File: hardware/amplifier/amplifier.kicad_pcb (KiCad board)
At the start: 2 copper layers, 52.4 x 41.4 mm, 13 parts, among them K1 Out, P1 Sensor, P2 Pwr, U1 AD8223, U2 LT1010

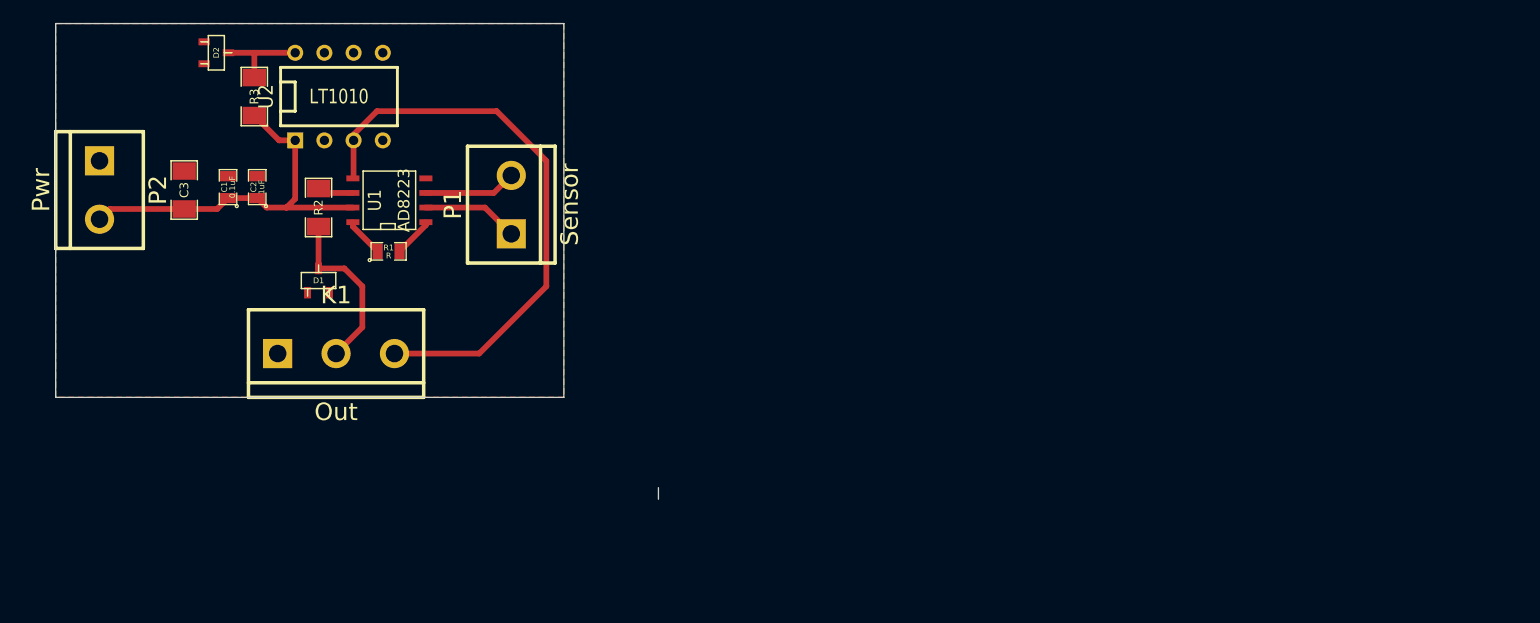
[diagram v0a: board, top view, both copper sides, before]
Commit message: Amplifier board: change instrumentation amplifier for INA2128.
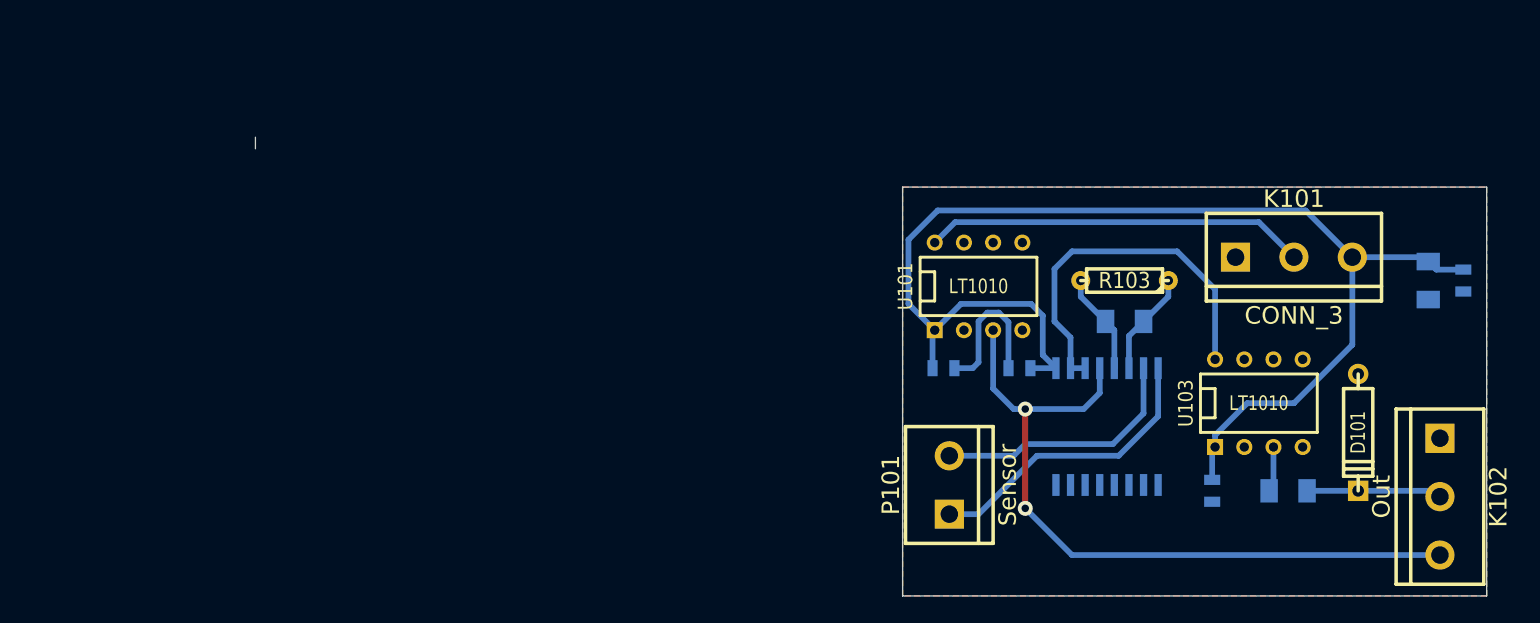
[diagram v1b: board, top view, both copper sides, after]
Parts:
- removed C1: 0.1uF, SM0805
- removed C2: 1uF, SM0805
- removed C3: 10uF, SM1206
- removed D1, D2: ZENER, sot23
- removed K1: Out, bornier3
- removed P1: Sensor, bornier2
- removed P2: Pwr, bornier2
- removed R1: R, SM0805
- removed R2, R3: 10K, SM1206
- removed U1: AD8223, SO8N
- removed U2: LT1010, DIP-8__300
- added C101: 0.1uF, SM0805, B.Cu at (296.2, 144.3)
- added C102: 1uF, SM0805, B.Cu at (318.0, 126.0)
- added C103: 10uF, SM1206, B.Cu at (315.0, 126.0)
- added C104: 0.1uF, SM0805, B.Cu at (279.4, 133.6)
- added C105: 0.1uF, SM0805, B.Cu at (272.8, 133.6)
- added D101: 1N4732, D4, F.Cu at (308.9, 139.2)
- added K101: CONN_3, bornier3, F.Cu at (303.3, 124.0)
- added K102: Out, bornier3, F.Cu at (316.0, 144.8)
- added P101: Sensor, bornier2, F.Cu at (273.3, 143.8)
- added R101: 1K, SM1206, B.Cu at (302.8, 144.3)
- added R102: R, SM1206, B.Cu at (288.5, 129.5)
- added R103: R, R3-LARGE_PADS, F.Cu at (288.5, 126.0)
- added U101: LT1010, DIP-8__300, F.Cu at (275.8, 126.5)
- added U102: INA2128, SO16L, B.Cu at (287.0, 138.7)
- added U103: LT1010, DIP-8__300, F.Cu at (300.2, 136.7)
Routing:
- net VDD: track 33.7 -> 108.5 mm
- net /VrefIN: track 0.00 -> 33.2 mm
- net N-000006: track 0.00 -> 32.5 mm
- net /Se2: track 8.38 -> 25.9 mm
- net /Vref: track 49.8 -> 64.2 mm, vias 0 -> 2
- net /Se1: track 8.06 -> 22.4 mm
- net GND: track 0.00 -> 13.1 mm
- net N-0000027: track 0.00 -> 9.04 mm
- net N-0000024: track 0.00 -> 8.83 mm
- net N-0000010: track 7.96 -> 0.00 mm
- net N-0000015: track 0.00 -> 3.97 mm
- net N-000002: track 3.49 -> 0.00 mm
- net N-000004: track 3.43 -> 0.00 mm
- net N-000001: track 3.14 -> 0.00 mm
- net /Vout: track 14.9 -> 11.8 mm
- added copper zone on B.Cu, net GND
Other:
- board size 52.4 x 41.4 mm -> 107.1 x 39.9 mm
- net class Default: via_dia 0.889 -> 1.3005; via_drill 0.635 -> 0.8992

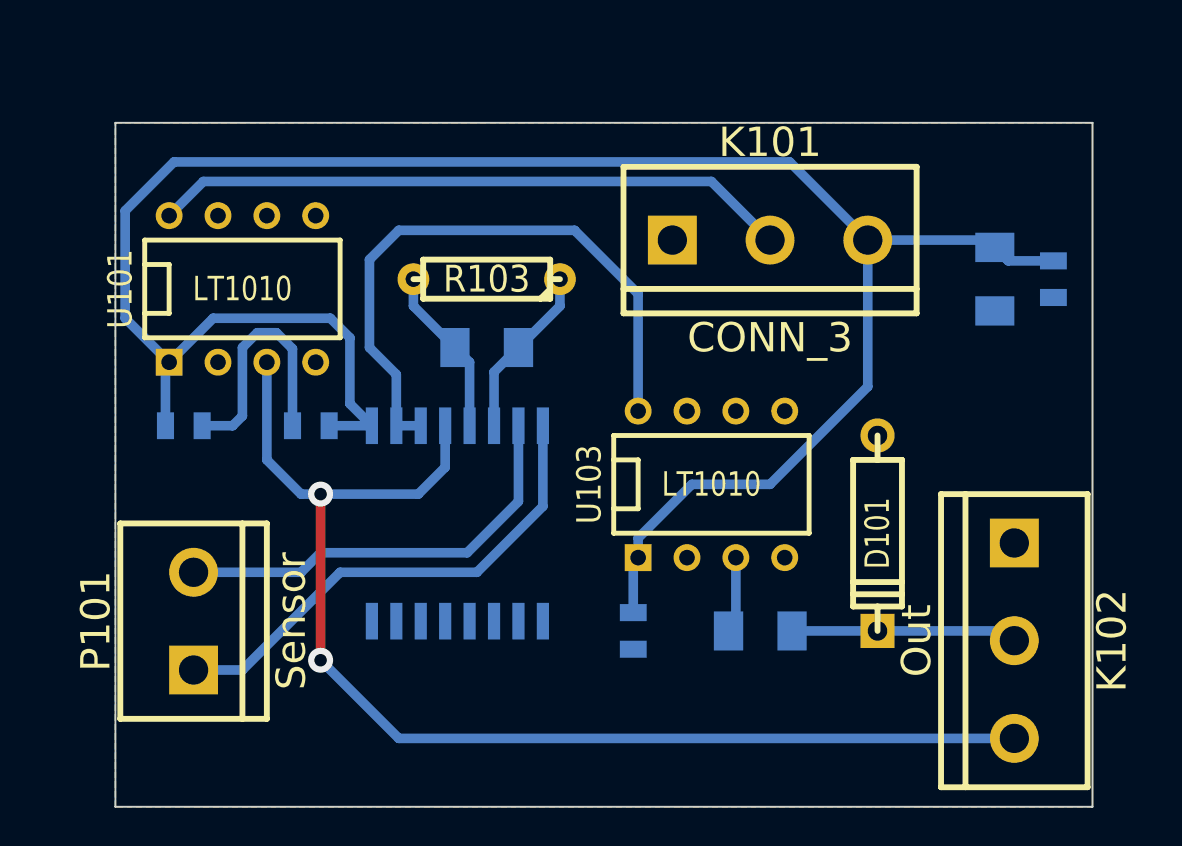
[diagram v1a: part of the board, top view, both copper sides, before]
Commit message: Moved power connector.
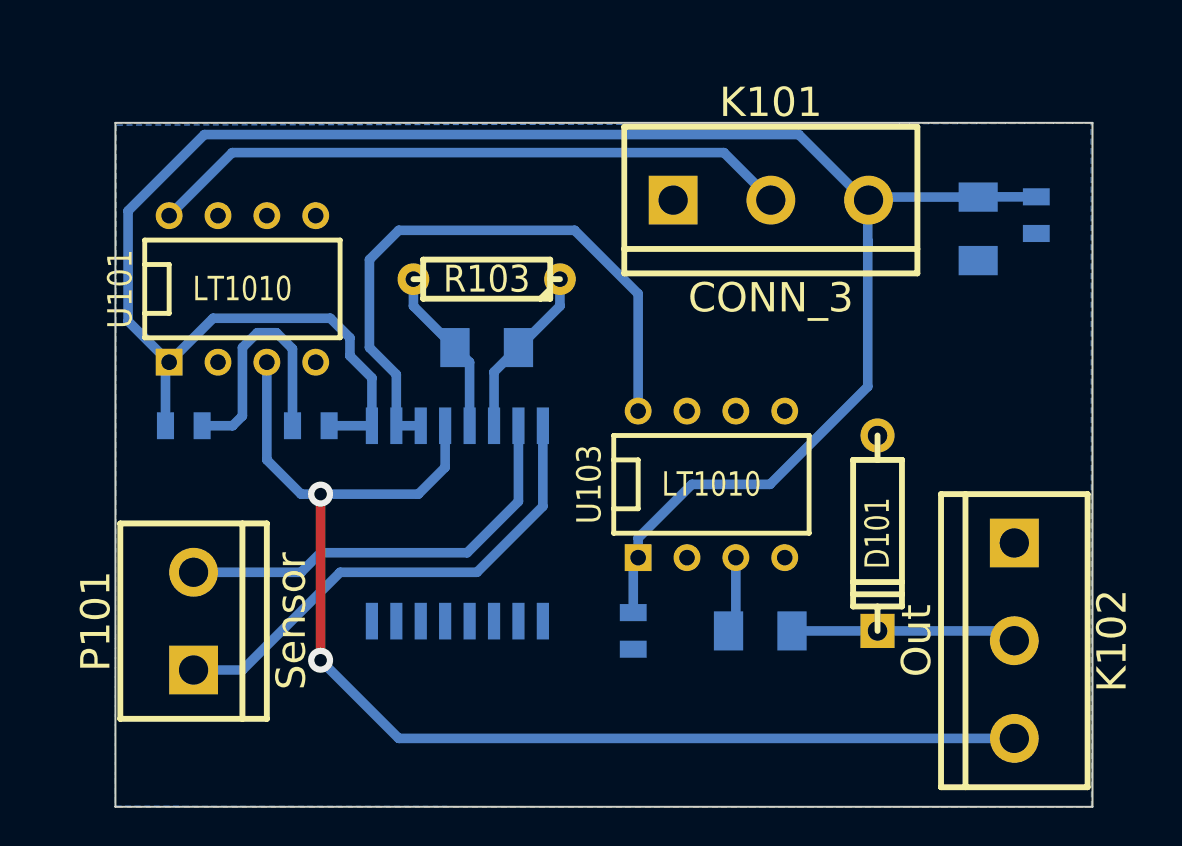
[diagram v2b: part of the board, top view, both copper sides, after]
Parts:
- moved C102 3.44 mm to (317.1, 122.7)
- moved C103 2.76 mm to (314.1, 123.4)
- moved K101 2.08 mm to (303.3, 121.9)
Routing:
- net VDD: track 108.5 -> 109.8 mm
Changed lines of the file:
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@@
-(kicad_pcb (version 3) (host pcbnew "(2013-jul-07)-stable")
+(kicad_pcb (version 3) (host pcbnew "(2013-07-07 BZR 4022)-stable")
   (general
     (links 32)
     (no_connects 0)
-    (area 212.897999 113.469999 212.998001 114.570001)
+    (area 212.897999 110.942001 335.66 153.466001)
     (thickness 1.6)
     (drawings 7)
-    (tracks 76)
+    (tracks 82)
     (zones 0)
     (modules 15)
@@
   (page A3)
   (layers
-    (15 F.Cu signal)
+    (15 F.Cu signal hide)
     (0 B.Cu signal)
     (16 B.Adhes user)
@@
   )
   (module SM1206 (layer B.Cu)
-    (at 314.96 125.984 270)
+    (at 314.0964 123.3678 270)
     (attr smd)
     (fp_text reference C103 (at 0 0 270) (layer B.SilkS)
@@
   )
   (module SM0805 (layer B.Cu)
-    (at 318.008 125.984 270)
+    (at 317.119 122.6566 270)
     (attr smd)
     (fp_text reference C102 (at 0 0.3175 270) (layer B.SilkS)
@@
   )
   (module bornier3 (layer F.Cu)
-    (at 303.276 123.952)
+    (at 303.31664 121.87428)
     (descr "Bornier d'alimentation 3 pins")
     (tags DEV)
@@
   (segment (start 279.908 137.16) (end 284.988 137.16) (width 0.5) (layer B.Cu) (net 4))
   (segment (start 277.114 135.382) (end 278.892 137.16) (width 0.5) (layer B.Cu) (net 4))
-  (segment (start 272.034 122.682) (end 273.812 120.904) (width 0.5) (layer B.Cu) (net 5))
-  (segment (start 300.228 120.904) (end 303.276 123.952) (width 0.5) (layer B.Cu) (net 5))
-  (segment (start 273.812 120.904) (end 300.228 120.904) (width 0.5) (layer B.Cu) (net 5))
+  (segment (start 303.31664 121.87428) (end 303.31664 121.8438) (width 0.5) (layer B.Cu) (net 5))
+  (segment (start 275.3106 119.4054) (end 272.034 122.682) (width 0.5) (layer B.Cu) (net 5))
+  (segment (start 300.87824 119.4054) (end 275.3106 119.4054) (width 0.5) (layer B.Cu) (net 5))
+  (segment (start 303.31664 121.8438) (end 300.87824 119.4054) (width 0.5) (layer B.Cu) (net 5))
   (segment (start 278.4475 133.604) (end 278.4475 129.6035) (width 0.5) (layer B.Cu) (net 6))
   (segment (start 275.336 133.604) (end 273.7485 133.604) (width 0.5) (layer B.Cu) (net 6))
@@
   (segment (start 293.116 123.444) (end 283.972 123.444) (width 0.5) (layer B.Cu) (net 10))
   (segment (start 296.418 126.746) (end 293.116 123.444) (width 0.5) (layer B.Cu) (net 10))
-  (segment (start 318.008 125.0315) (end 315.6585 125.0315) (width 0.5) (layer B.Cu) (net 11))
-  (segment (start 315.6585 125.0315) (end 314.96 124.333) (width 0.5) (layer B.Cu) (net 11))
-  (segment (start 308.356 123.952) (end 314.579 123.952) (width 0.5) (layer B.Cu) (net 11))
-  (segment (start 314.579 123.952) (end 314.96 124.333) (width 0.5) (layer B.Cu) (net 11))
-  (segment (start 272.034 130.302) (end 269.748 128.016) (width 0.5) (layer B.Cu) (net 11))
-  (segment (start 304.292 119.888) (end 308.356 123.952) (width 0.5) (layer B.Cu) (net 11))
-  (segment (start 272.288 119.888) (end 304.292 119.888) (width 0.5) (layer B.Cu) (net 11))
-  (segment (start 269.748 122.428) (end 272.288 119.888) (width 0.5) (layer B.Cu) (net 11))
-  (segment (start 269.748 128.016) (end 269.748 122.428) (width 0.5) (layer B.Cu) (net 11))
-  (segment (start 272.034 130.302) (end 274.32 128.016) (width 0.5) (layer B.Cu) (net 11))
-  (segment (start 281.432 132.461) (end 282.575 133.604) (width 0.5) (layer B.Cu) (net 11))
-  (segment (start 281.432 129.032) (end 281.432 132.461) (width 0.5) (layer B.Cu) (net 11))
+  (segment (start 308.39664 121.87428) (end 308.1782 121.87428) (width 0.5) (layer B.Cu) (net 11))
+  (segment (start 269.9004 128.1684) (end 272.034 130.302) (width 0.5) (layer B.Cu) (net 11))
+  (segment (start 269.9004 122.43308) (end 269.9004 128.1684) (width 0.5) (layer B.Cu) (net 11))
+  (segment (start 273.86788 118.4656) (end 269.9004 122.43308) (width 0.5) (layer B.Cu) (net 11))
+  (segment (start 304.76952 118.4656) (end 273.86788 118.4656) (width 0.5) (layer B.Cu) (net 11))
+  (segment (start 308.1782 121.87428) (end 304.76952 118.4656) (width 0.5) (layer B.Cu) (net 11))
+  (segment (start 314.0964 121.7168) (end 308.55412 121.7168) (width 0.5) (layer B.Cu) (net 11))
+  (segment (start 308.55412 121.7168) (end 308.39664 121.87428) (width 0.5) (layer B.Cu) (net 11))
+  (segment (start 317.119 121.7041) (end 314.1091 121.7041) (width 0.5) (layer B.Cu) (net 11))
+  (segment (start 314.1091 121.7041) (end 314.0964 121.7168) (width 0.5) (layer B.Cu) (net 11))
+  (segment (start 308.356 124.38888) (end 308.356 121.91492) (width 0.5) (layer B.Cu) (net 11))
+  (segment (start 308.356 121.91492) (end 308.39664 121.87428) (width 0.5) (layer B.Cu) (net 11))
+  (segment (start 296.418 140.462) (end 296.418 139.446) (width 0.5) (layer B.Cu) (net 11))
+  (segment (start 296.418 139.446) (end 299.212 136.652) (width 0.5) (layer B.Cu) (net 11))
+  (segment (start 299.212 136.652) (end 303.276 136.652) (width 0.5) (layer B.Cu) (net 11))
+  (segment (start 303.276 136.652) (end 308.356 131.572) (width 0.5) (layer B.Cu) (net 11))
+  (segment (start 308.356 131.572) (end 308.356 124.38888) (width 0.5) (layer B.Cu) (net 11))
+  (segment (start 308.356 124.38888) (end 308.356 123.952) (width 0.5) (layer B.Cu) (net 11))
+  (segment (start 282.575 133.604) (end 282.575 131.1148) (width 0.5) (layer B.Cu) (net 11))
+  (segment (start 281.432 129.032) (end 281.432 129.9718) (width 0.5) (layer B.Cu) (net 11))
   (segment (start 280.416 128.016) (end 281.432 129.032) (width 0.5) (layer B.Cu) (net 11))
   (segment (start 274.32 128.016) (end 280.416 128.016) (width 0.5) (layer B.Cu) (net 11))
+  (segment (start 272.034 130.302) (end 274.32 128.016) (width 0.5) (layer B.Cu) (net 11))
+  (segment (start 282.575 131.1148) (end 281.432 129.9718) (width 0.5) (layer B.Cu) (net 11))
   (segment (start 271.8435 133.604) (end 271.8435 130.4925) (width 0.5) (layer B.Cu) (net 11))
   (segment (start 271.8435 130.4925) (end 272.034 130.302) (width 0.5) (layer B.Cu) (net 11))
   (segment (start 282.575 133.604) (end 280.3525 133.604) (width 0.5) (layer B.Cu) (net 11))
-  (segment (start 296.418 140.462) (end 296.418 139.446) (width 0.5) (layer B.Cu) (net 11))
-  (segment (start 308.356 131.572) (end 308.356 123.952) (width 0.5) (layer B.Cu) (net 11))
-  (segment (start 303.276 136.652) (end 308.356 131.572) (width 0.5) (layer B.Cu) (net 11))
-  (segment (start 299.212 136.652) (end 303.276 136.652) (width 0.5) (layer B.Cu) (net 11))
-  (segment (start 296.418 139.446) (end 299.212 136.652) (width 0.5) (layer B.Cu) (net 11))
   (segment (start 296.164 143.3195) (end 296.164 140.716) (width 0.5) (layer B.Cu) (net 11))
   (segment (start 296.164 140.716) (end 296.418 140.462) (width 0.5) (layer B.Cu) (net 11))
-  (zone (net 6) (net_name GND) (layer B.Cu) (hatch edge 0.508)
-    (connect_pads (clearance 0.508))
-    (min_thickness 0.254)
-    (fill (arc_segments 16) (thermal_gap 0.5) (thermal_bridge_width 0.5))
-    (polygon
-      (pts
-        (xy 320.04 153.416) (xy 269.24 153.416) (xy 269.24 117.856) (xy 320.04 117.856)
-      )
-    )
-  )
   (zone (net 6) (net_name GND) (layer F.Cu) (hatch edge 0.508)
     (connect_pads (clearance 0.508))
@@
       )
     )
+  )
+  (zone (net 6) (net_name GND) (layer B.Cu) (hatch edge 0.508)
+    (connect_pads (clearance 0.508))
+    (min_thickness 0.254)
+    (fill (arc_segments 16) (thermal_gap 0.508) (thermal_bridge_width 0.508))
+    (polygon
+      (pts
+        (xy 320.04 117.8814) (xy 269.28064 117.97284) (xy 269.24 153.3906) (xy 319.9892 153.42616) (xy 319.96888 117.91696)
+        (xy 320.00444 117.91696)
+      )
+    )
